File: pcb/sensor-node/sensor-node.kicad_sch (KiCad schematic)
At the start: 0 parts

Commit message: chore: Add RAK3172 symbol, fp, 3d model
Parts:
- added U1: RAK3172-xx-8-SM-xI, RF_Module:RAK3172, symbol RF_Module:RAK3172-xx-8-SM-xI
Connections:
- new net: U1.11 (GND), U1.17 (GND), U1.18 (GND), U1.23 (GND), U1.28 (GND)
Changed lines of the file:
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@@
 	(generator_version "10.0")
 	(paper "A4")
+	(symbol
+		(lib_id "RF_Module:RAK3172-xx-8-SM-xI")
+		(at 143.51 92.71 0)
+		(unit 1)
+		(body_style 1)
+		(exclude_from_sim no)
+		(in_bom yes)
+		(on_board yes)
+		(in_pos_files yes)
+		(dnp no)
+		(fields_autoplaced yes)
+		(property "Reference" "U1"
+			(at 145.9563 62.23 0)
+			(show_name no)
+			(do_not_autoplace no)
+			(effects
+				(font
+					(size 1.27 1.27)
+				)
+				(justify left)
+			)
+		)
+		(property "Value" "RAK3172-xx-8-SM-xI"
+			(at 145.9563 64.77 0)
+			(show_name no)
+			(do_not_autoplace no)
+			(effects
+				(font
+					(size 1.27 1.27)
+				)
+				(justify left)
+			)
+		)
+		(property "Footprint" "RF_Module:RAK3172"
+			(at 143.51 137.922 0)
+			(hide yes)
+			(show_name no)
+			(do_not_autoplace no)
+			(effects
+				(font
+					(size 1.27 1.27)
+				)
+				(justify bottom)
+			)
+		)
+		(property "Datasheet" "https://docs.rakwireless.com/Product-Categories/WisDuo/RAK3172-Module/Datasheet/"
+			(at 143.764 133.858 0)
+			(hide yes)
+			(show_name no)
+			(do_not_autoplace no)
+			(effects
+				(font
+					(size 1.27 1.27)
+				)
+				(justify bottom)
+			)
+		)
+		(property "Description" "LoRa Module, STM32WLE5, RU864/IN865/EU868, RAKwireless"
+			(at 143.764 135.382 0)
+			(hide yes)
+			(show_name no)
+			(do_not_autoplace no)
+			(effects
+				(font
+					(size 1.27 1.27)
+				)
+			)
+		)
+		(pin "24"
+		)
+		(pin "15"
+		)
+		(pin "14"
+		)
+		(pin "25"
+		)
+		(pin "23"
+		)
+		(pin "22"
+		)
+		(pin "17"
+		)
+		(pin "16"
+		)
+		(pin "18"
+		)
+		(pin "28"
+		)
+		(pin "26"
+		)
+		(pin "31"
+		)
+		(pin "32"
+		)
+		(pin "10"
+		)
+		(pin "9"
+		)
+		(pin "7"
+		)
+		(pin "11"
+		)
+		(pin "12"
+		)
+		(pin "8"
+		)
+		(pin "13"
+		)
+		(pin "1"
+		)
+		(pin "2"
+		)
+		(pin "6"
+		)
+		(pin "19"
+		)
+		(pin "20"
+		)
+		(pin "21"
+		)
+		(pin "27"
+		)
+		(pin "29"
+		)
+		(pin "30"
+		)
+		(pin "3"
+		)
+		(pin "4"
+		)
+		(pin "5"
+		)
+		(instances
+			(project "sensor-node"
+				(path "/d9feb3bd-92db-4b5c-afb9-657d4a22d415"
+					(reference "U1")
+					(unit 1)
+				)
+			)
+		)
+	)
 	(sheet_instances
 		(path "/"

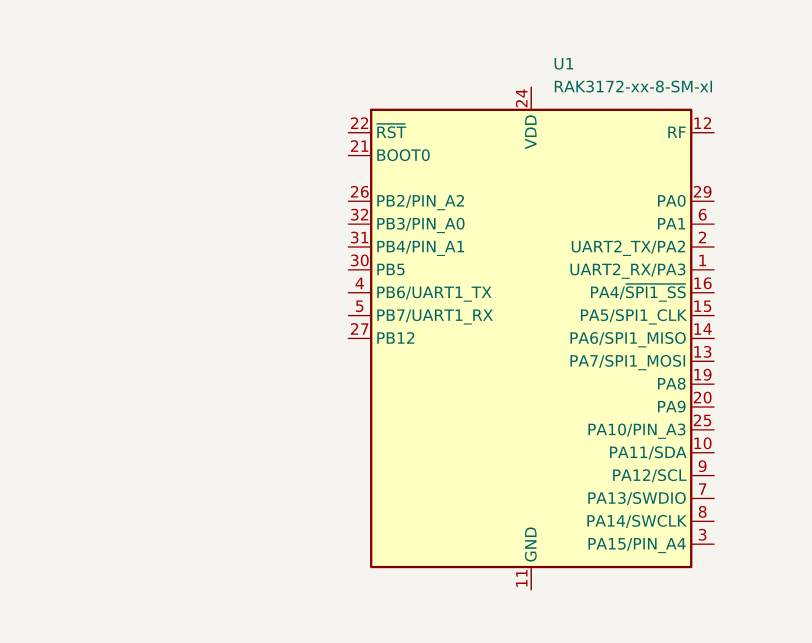
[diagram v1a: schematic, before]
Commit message: schematic: Add RAK3172 reset stuff
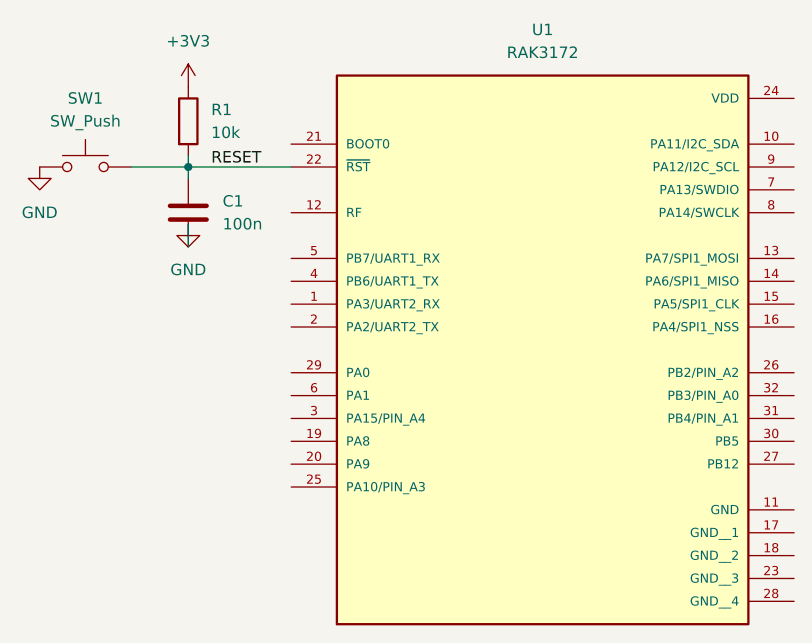
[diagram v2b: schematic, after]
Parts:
- removed U1: RAK3172-xx-8-SM-xI, RF_Module:RAK3172, symbol RF_Module:RAK3172-xx-8-SM-xI
- added C1: 100n, symbol Device:C
- added R1: 10k, RAK3172:XCVR_RAK3172, symbol Device:R
- added SW1: SW_Push, Package_TO_SOT_SMD:TO-263-7_TabPin8, symbol Switch:SW_Push
- added U1: RAK3172, RAK3172:XCVR_RAK3172, symbol RAK3172:RAK3172
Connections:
- new net +3V3: R1.1
- new net GND: C1.2, SW1.1
- new net RESET: C1.1, R1.2, SW1.2, U1.22 (~{RST})
